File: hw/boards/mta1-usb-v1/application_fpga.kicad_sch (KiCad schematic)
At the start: 38 parts, among them U10 PT2043AT6, U6 ICE40UP5K-SG48ITR, U8 W25Q80DVUXIE

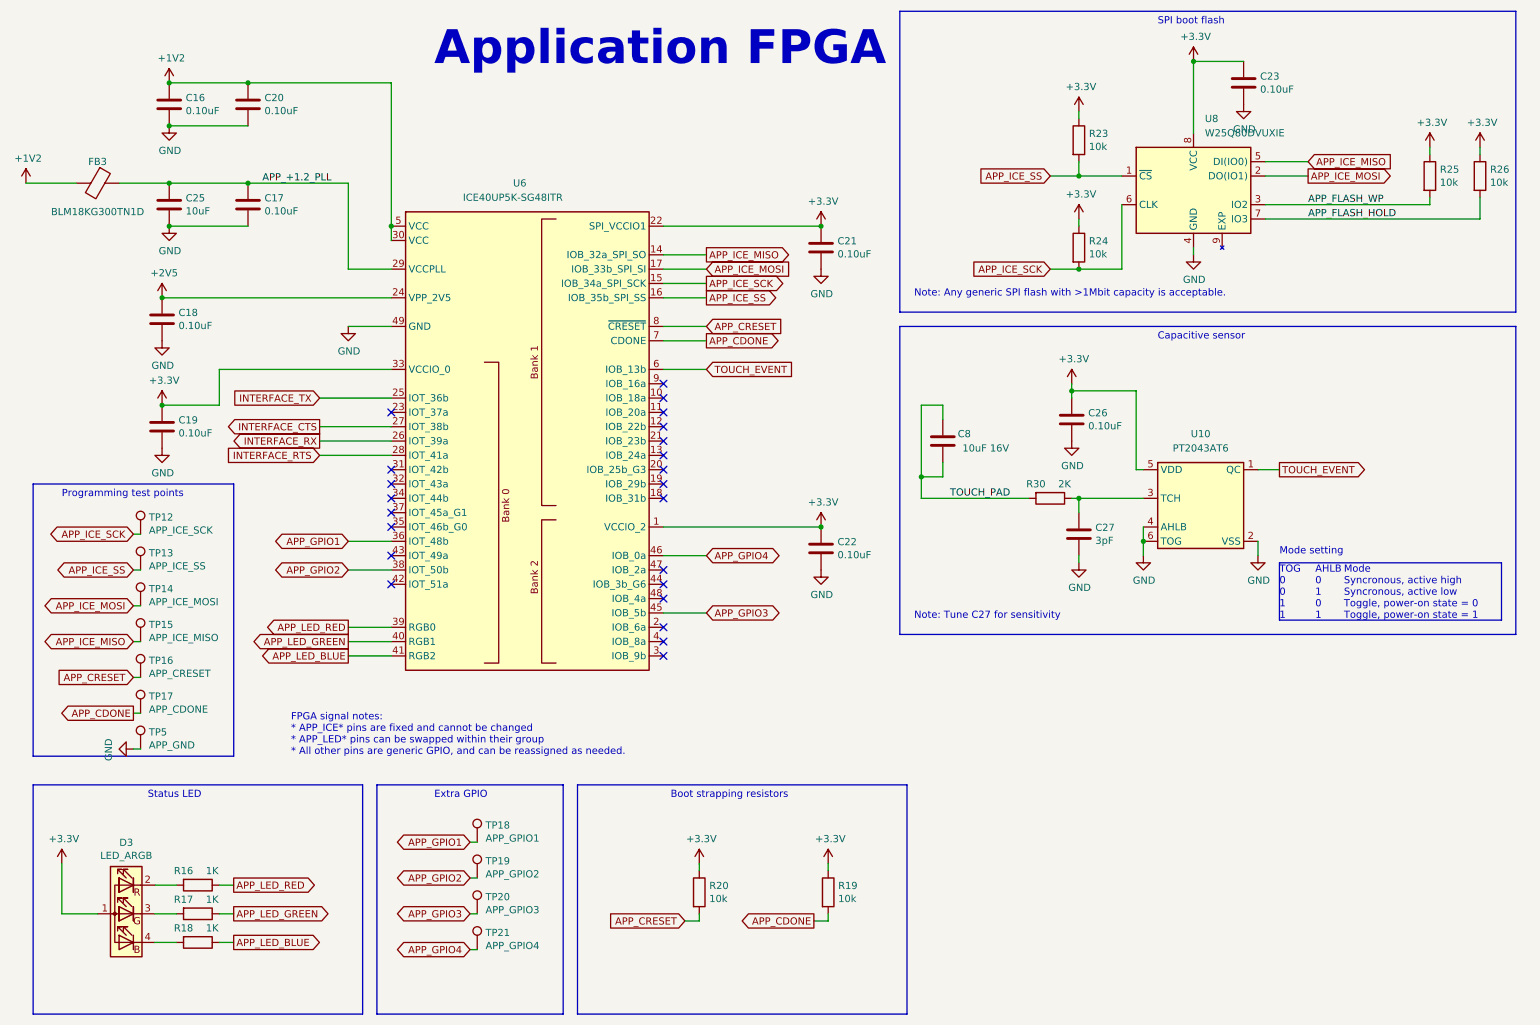
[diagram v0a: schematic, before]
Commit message: TK-1 and TP-1 PCBs (#52)
* Add kicad library for flat programming clip

* Add descriptions to part symbols

* Add extended values, manufacturer/distributor info to components in mta1

* Add new board entry for TK1

* Add TP1 programmer design

* Update MTA1-USB-V1 release files to match production

* Change SPI flash memory type to XT25F08BDFIGT-S
* Change touch sensor feedback cap to 1uF
* Add manufacturer, manufacturer part number, distributor, distributor part number

* Update component values for TK1 PCB

* Use specific part # for C8
* Change flash back to Winbond part, for easier sourcing
* Change C1 to 1pF

* Fixes for production programmer PCB

* Swap GND and 5V on J3
* Replace graphic logo with text
* Rename part to 'TP-1'

* TK-1 release

* Add dimensions for PCB
* Add layer stackup for PCB
* Change PCB component origin to match expanded board
* Change schematic title to 'TK-1', update release date

* mta1-usb-v1-programmer: Add corrected part numbers for OSFC production

* Q1, Q2, F1 part subsititutions
* add mfr/supplier info for all parts

* PCB library: add parts

* Rectangular footprint for TK-1 test pads
* BOM generation script used for TK-1 and TP-1 releases

* TP-1 release

* Schematic: Add manufacturer, supplier information for all parts
* Schematic: Update name and release date
* PCB: Add PCB fabrication information
* PCB: Correct pinouts on silkscreen

* PCB library: add 'screw' and 'foot' symbols

* Screw is a schematic-only part, for including mechanical screws in the
  BOM
* Foot is for self-adhesive rubber mounting feet that can be stuck to
  the bottom of a PCB

* TP-1 release: Add screws, feet to the BOM

* Pico library: Add footprint for RPi Pico w/solder paste

* TP-1 RevA release updates:

* Add fiducials in 3 corners (1mm exposed copper ring w/2mm soldermask opening)
* Add solder paste openings to Raspberry Pi Pico pads

* TK-1: RevA.1 release

* Add two fiducials to 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
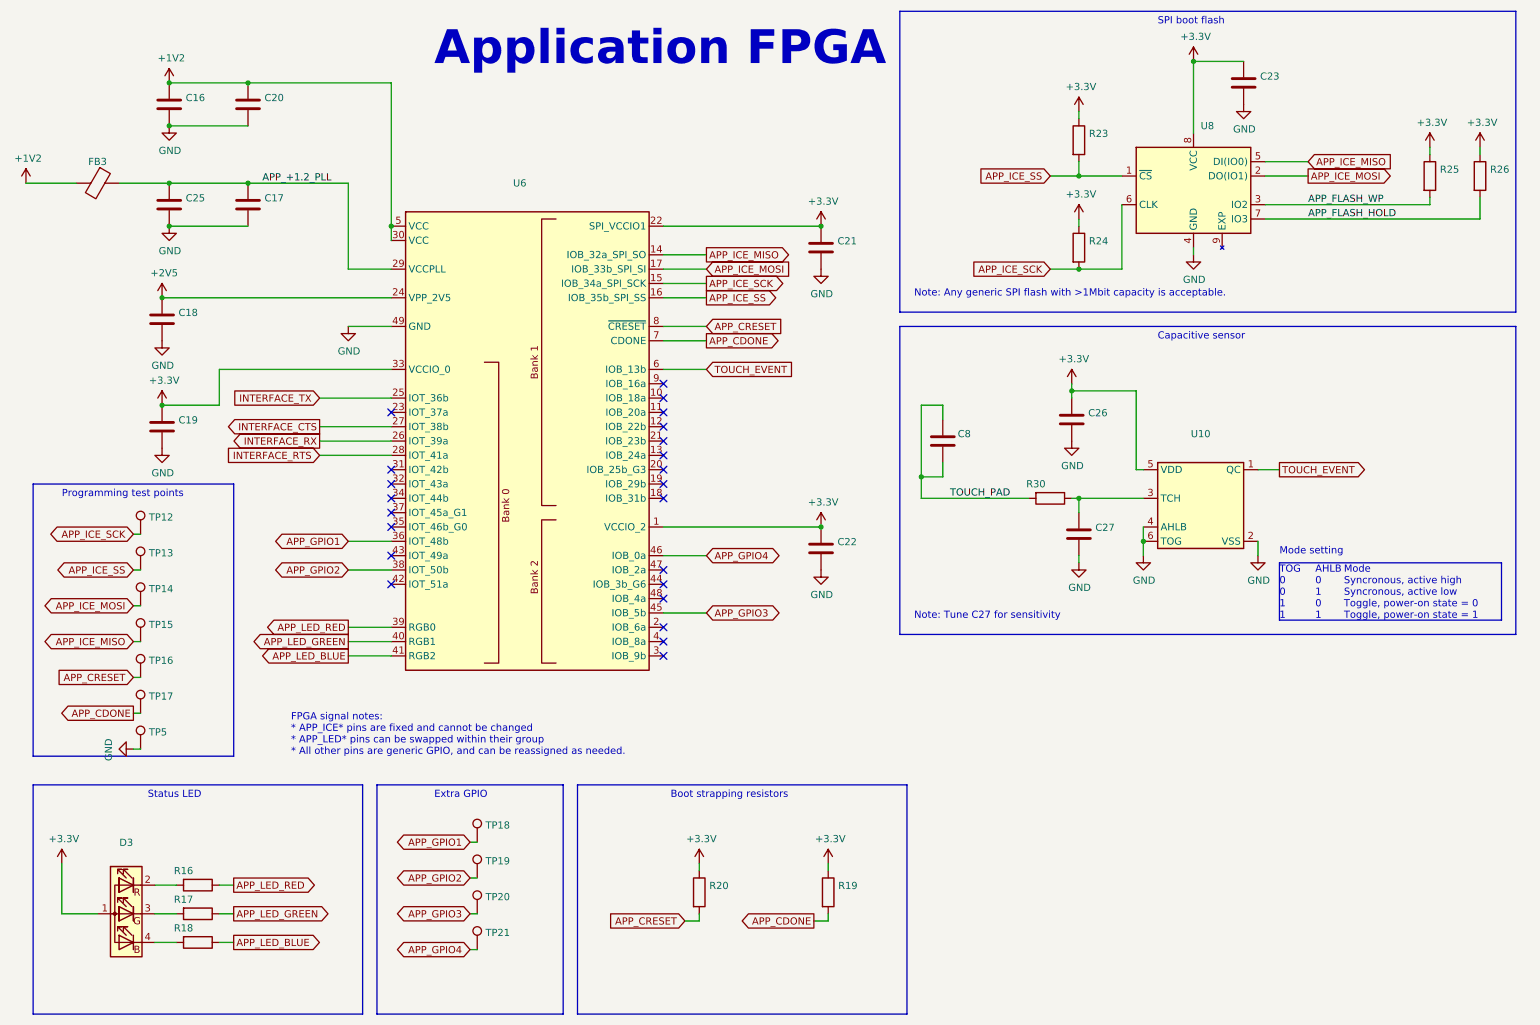
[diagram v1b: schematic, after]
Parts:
- C16, C17, C18, C19, C20, C21, C22, C23, C26: value 0.10uF -> (none); footprint mta1:CAPC1005X06L -> (none); Extended Value (none) -> 16V,X5R,20%; Manufacturer (none) -> Any/not critical
- C25: value 10uF -> (none); footprint mta1:CAPC1608X09L -> (none); Extended Value (none) -> 10V,X5R,20%; Manufacturer (none) -> Any/not critical
- C27: value 3pF -> (none); footprint mta1:CAPC1005X06L -> (none); Extended Value (none) -> 16V,X5R,20%; Manufacturer (none) -> Any/not critical
- C8: value 10uF 16V -> (none); footprint Capacitor_SMD:C_1206_3216Metric -> (none); Extended Value (none) -> 16V,X5R,10%; Manufacturer (none) -> Fenghua; Manufacturer Part Number (none) -> 1206X106K160NT; Supplier (none) -> LCSC; Supplier Part Number (none) -> C105478
- D3: value LED_ARGB -> (none); footprint mta1:0402rgb-1010 -> (none); Manufacturer (none) -> Foshan NationStar; Manufacturer Part Number (none) -> FC-B1010RGBT-HG; Supplier (none) -> LCSC; Supplier Part Number (none) -> C158099
- FB3: value BLM18KG300TN1D -> (none); footprint mta1:Ferritbead_0603_1608Metric -> (none); Manufacturer (none) -> Murata; Manufacturer Part Number (none) -> BLM18KG300TN1D; Supplier (none) -> Digikey; Supplier Part Number (none) -> 490-5447-1-ND
- R16, R17, R18: value 1K -> (none); footprint mta1:ERJ2G(0402)_L -> (none); Extended Value (none) -> 1/16W,5%; Manufacturer (none) -> Any/not critical
- R19, R20, R23, R24, R25, R26: value 10k -> (none); footprint mta1:ERJ2G(0402)_L -> (none); Extended Value (none) -> 1/16W,5%; Manufacturer (none) -> Any/not critical
- R30: value 2K -> (none); footprint mta1:ERJ2G(0402)_L -> (none); Extended Value (none) -> 1/16W,1%; Manufacturer (none) -> Any/not critical
- TP12: value APP_ICE_SCK -> (none); footprint TestPoint:TestPoint_Pad_D1.0mm -> (none); now left out of the parts list
- TP13: value APP_ICE_SS -> (none); footprint TestPoint:TestPoint_Pad_D1.0mm -> (none); now left out of the parts list
- TP14: value APP_ICE_MOSI -> (none); footprint TestPoint:TestPoint_Pad_D1.0mm -> (none); now left out of the parts list
- TP15: value APP_ICE_MISO -> (none); footprint TestPoint:TestPoint_Pad_D1.0mm -> (none); now left out of the parts list
- TP16: value APP_CRESET -> (none); footprint TestPoint:TestPoint_Pad_D1.0mm -> (none); now left out of the parts list
- TP17: value APP_CDONE -> (none); footprint TestPoint:TestPoint_Pad_D1.0mm -> (none); now left out of the parts list
- TP18: value APP_GPIO1 -> (none); footprint TestPoint:TestPoint_Pad_D1.0mm -> (none); now left out of the parts list
- TP19: value APP_GPIO2 -> (none); footprint TestPoint:TestPoint_Pad_D1.0mm -> (none); now left out of the parts list
- TP20: value APP_GPIO3 -> (none); footprint TestPoint:TestPoint_Pad_D1.0mm -> (none); now left out of the parts list
- TP21: value APP_GPIO4 -> (none); footprint TestPoint:TestPoint_Pad_D1.0mm -> (none); now left out of the parts list
- TP5: value APP_GND -> (none); footprint TestPoint:TestPoint_Pad_D1.0mm -> (none); now left out of the parts list
- U10: value PT2043AT6 -> (none); footprint Package_TO_SOT_SMD:SOT-23-6 -> (none); Manufacturer (none) -> PinTeng; Manufacturer Part Number (none) -> PT2043AT6; Supplier (none) -> LCSC; Supplier Part Number (none) -> C2914233
- U6: value ICE40UP5K-SG48ITR -> (none); footprint Package_DFN_QFN:QFN-48-1EP_7x7mm_P0.5mm_EP5.6x5.6mm -> (none); Manufacturer (none) -> Lattice; Manufacturer Part Number (none) -> ICE40UP5K-SG48ITR; Supplier (none) -> Digikey; Supplier Part Number (none) -> 220-2145-2-ND
- U8: value W25Q80DVUXIE -> (none); footprint mta1:W25Q80DVUXIE -> (none); Manufacturer (none) -> XTX; Manufacturer Part Number (none) -> XT25F08BDFIGT-S; Supplier (none) -> LCSC; Supplier Part Number (none) -> C558860
